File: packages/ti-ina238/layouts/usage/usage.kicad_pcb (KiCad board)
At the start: 2 copper layers, 5 parts

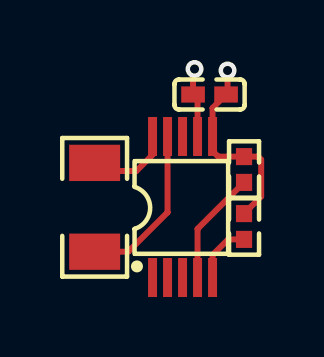
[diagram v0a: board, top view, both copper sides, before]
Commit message: ti-ina238: package update to v0.2.0, ato:^0.14.0
Build targets:
  default = rc0
  usage = rc0
Package Verify: rc0
Version: 0.1.2 -> 0.2.0
Requires ato: ^0.14.0
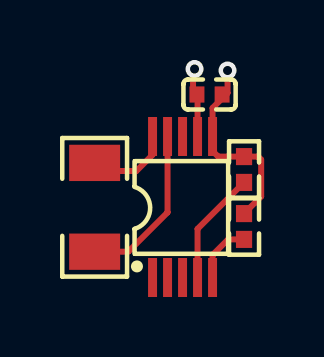
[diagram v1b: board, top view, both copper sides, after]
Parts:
- C1: value 100nF ±10% 16V X7R -> 1±10.0%F
- R1: value 16mΩ ±1% 1W -> 10000±1.0%Ω
- R2, R3: value 10kΩ ±1% 62.5mW -> 10000±1.0%Ω
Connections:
- net power_in-VCC renamed i2c_P
- net power_out-VCC renamed load_N
- C1 pad 2: GND -> lv
- U1 pad 1: address_bit_1 -> lv
- U1 pad 2: address_bit_0 -> lv
- U1 pad 7: GND -> lv
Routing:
- net GND: track 2.33 -> 0.00 mm, vias 1 -> 0
- net 1: track 0.00 -> 2.33 mm, vias 0 -> 1

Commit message: fixed literal bugs
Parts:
- removed C1: 1±10.0%F, Samsung_Electro_Mechanics_CL05B104KO5NNNC:C0402
- R1: value 10000±1.0%Ω -> 16mΩ
- R2, R3: value 10000±1.0%Ω -> 10kΩ
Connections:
- net load_N renamed INneg_N
- R1 pad 1: i2c_P -> INpos_P
- R2 pad 2: i2c_P -> hv
- R3 pad 2: i2c_P -> hv
- U1 pad 10: i2c_P -> INpos_P
- U1 pad 6: i2c_P -> hv
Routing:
- net i2c_P: track 9.54 -> 0.00 mm, vias 1 -> 0
- net hv: track 0.00 -> 9.54 mm, vias 0 -> 1
- net INpos_P: track 0.00 -> 2.33 mm, vias 0 -> 1
- net 1: track 2.33 -> 0.00 mm, vias 1 -> 0

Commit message: rebuild for frozen
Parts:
- R1: value 16mΩ -> 0.016Ω
- R2, R3: value 10kΩ -> 10000Ω
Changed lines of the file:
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@@
 	)
 	(setup
+		(stackup
+			(layer "F.SilkS"
+				(type "Top Silk Screen")
+			)
+			(layer "F.Paste"
+				(type "Top Solder Paste")
+			)
+			(layer "F.Mask"
+				(type "Top Solder Mask")
+				(color "Black")
+				(thickness 0.01)
+				(material "Solder mask")
+				(epsilon_r 3.3)
+			)
+			(layer "F.Cu"
+				(type "copper")
+				(thickness 0.035)
+			)
+			(layer "dielectric 1"
+				(type "core")
+				(thickness 1.51)
+				(material "FR4")
+				(epsilon_r 4.5)
+				(loss_tangent 0.02)
+			)
+			(layer "B.Cu"
+				(type "copper")
+				(thickness 0.035)
+			)
+			(layer "B.Mask"
+				(type "Bottom Solder Mask")
+				(color "Black")
+				(thickness 0.01)
+				(material "Solder mask")
+				(epsilon_r 3.3)
+			)
+			(layer "B.Paste"
+				(type "Bottom Solder Paste")
+			)
+			(layer "B.SilkS"
+				(type "Bottom Silk Screen")
+			)
+			(copper_finish "ENIG")
+		)
 		(pad_to_mask_clearance 0)
 		(allow_soldermask_bridges_in_footprints no)
@@
 			)
 		)
-		(property "Value" "10kΩ"
+		(property "Value" "10000Ω"
 			(at 0 4 90)
 			(layer "F.Fab")
@@
 			)
 		)
-		(property "resistance" "10±1.0%kΩ"
-			(at 0 0 0)
-			(layer "User.9")
-			(hide yes)
-		)
-		(property "max_power" "62.5mW"
+		(property "resistance" "10000±1.0%Ω"
+			(at 0 0 0)
+			(layer "User.9")
+			(hide yes)
+		)
+		(property "max_power" "0.062W"
 			(at 0 0 0)
 			(layer "User.9")
@@
 			)
 		)
-		(property "Value" "10kΩ"
+		(property "Value" "10000Ω"
 			(at 0 4 90)
 			(layer "F.Fab")
@@
 			)
 		)
-		(property "resistance" "10±1.0%kΩ"
-			(at 0 0 0)
-			(layer "User.9")
-			(hide yes)
-		)
-		(property "max_power" "62.5mW"
+		(property "resistance" "10000±1.0%Ω"
+			(at 0 0 0)
+			(layer "User.9")
+			(hide yes)
+		)
+		(property "max_power" "0.062W"
 			(at 0 0 0)
 			(layer "User.9")
@@
 			)
 		)
-		(property "Value" "16mΩ"
+		(property "Value" "0.016Ω"
 			(at 0 4 270)
 			(layer "F.Fab")
@@
 			)
 		)
-		(property "resistance" "16±1.0%mΩ"
+		(property "resistance" "0.016±1.0%Ω"
 			(at 0 0 0)
 			(layer "User.9")
@@
 			(hide yes)
 		)
-		(property "max_voltage" "any ≥0V"
-			(at 0 0 0)
-			(layer "User.9")
+		(property "max_voltage" "ℝ+V"
+			(at 0 0 0)
+			(layer "User.9")

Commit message: catching up to main
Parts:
- added C1: 100nF ±10% 16V X7R, Samsung_Electro_Mechanics_CL05B104KO5NNNC:C0402, F.Cu at (152.0, 93.0)
- R1: value 0.016Ω -> 16mΩ ±1% 1W
- R2, R3: value 10000Ω -> 10kΩ ±1% 62.5mW
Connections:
- net INneg_N renamed power_out-VCC
- R1 pad 1: INpos_P -> power_in-VCC
- R2 pad 2: hv -> power_in-VCC
- R3 pad 2: hv -> power_in-VCC
- U1 pad 1: lv -> address_bit_1
- U1 pad 10: INpos_P -> power_in-VCC
- U1 pad 2: lv -> address_bit_0
- U1 pad 6: hv -> power_in-VCC
- U1 pad 7: lv -> GND
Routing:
- net power_in-VCC: track 0.00 -> 9.54 mm, vias 0 -> 1
- net hv: track 9.54 -> 0.00 mm, vias 1 -> 0
- net INpos_P: track 2.33 -> 0.00 mm, vias 1 -> 0
- net GND: track 0.00 -> 2.33 mm, vias 0 -> 1

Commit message: fix ti-ina238
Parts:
- C1: value 100nF ±10% 16V X7R -> 1.0000000000000001e-07F
- R1: value 16mΩ ±1% 1W -> 0.016Ω
- R2, R3: value 10kΩ ±1% 62.5mW -> 10000.0Ω
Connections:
- net power_in-VCC renamed <bound method has_net_name_affix.get_prefix of <has_net_name_affix '0x45F3B.sensor.shunt_input.net_name_suffixes[0]' on <Node[Electrical] '0x45F3B.sensor.shunt_input.p.line'>>>supply<bound method has_...Electrical] '0x45F3B.sensor.shunt_input.p.line'>>>
- net power_out-VCC renamed <bound method has_net_name_affix.get_prefix of <has_net_name_affix '0x45F3B.sensor.shunt_input.net_name_suffixes[1]' on <Node[Electrical] '0x45F3B.sensor.shunt_input.n.line'>>>load<bound method has_ne...Electrical] '0x45F3B.sensor.shunt_input.n.line'>>>
- C1 pad 2: GND -> lv
- U1 pad 1: address_bit_1 -> lv
- U1 pad 2: address_bit_0 -> lv
- U1 pad 7: GND -> lv
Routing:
- net GND: track 2.33 -> 0.00 mm, vias 1 -> 0
- net 1: track 0.00 -> 2.33 mm, vias 0 -> 1

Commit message: fix ti-ina238
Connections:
- net <bound method has_net_name_affix.get_prefix of <has_net_name_affix '0x45F3B.sensor.shunt_input.net_name_suffixes[0]' on <Node[Electrical] '0x45F3B.sensor.shunt_input.p.line'>>>supply<bound method has_...Electrical] '0x45F3B.sensor.shunt_input.p.line'>>> renamed supply_P
- net <bound method has_net_name_affix.get_prefix of <has_net_name_affix '0x45F3B.sensor.shunt_input.net_name_suffixes[1]' on <Node[Electrical] '0x45F3B.sensor.shunt_input.n.line'>>>load<bound method has_ne...Electrical] '0x45F3B.sensor.shunt_input.n.line'>>> renamed load_N
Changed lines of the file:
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@@
 	)
 	(net 2 "VBUS")
-	(net 3 "<bound method has_net_name_affix.get_prefix of <has_net_name_affix '0x45F3B.sensor.shunt_input.net_name_suffixes[1]' on <Node[Electrical] '0x45F3B.sensor.shunt_input.n.line'>>>load<bound method has_ne...Electrical] '0x45F3B.sensor.shunt_input.n.line'>>>")
+	(net 3 "load_N")
 	(net 4 "ALERT")
 	(net 6 "SCL")
 	(net 7 "SDA")
-	(net 9 "<bound method has_net_name_affix.get_prefix of <has_net_name_affix '0x45F3B.sensor.shunt_input.net_name_suffixes[0]' on <Node[Electrical] '0x45F3B.sensor.shunt_input.p.line'>>>supply<bound method has_...Electrical] '0x45F3B.sensor.shunt_input.p.line'>>>")
+	(net 9 "supply_P")
 	(net 10 "lv")
 	(footprint "Samsung_Electro_Mechanics_CL05B104KO5NNNC:C0402"
@@
 			(size 0.5 0.54)
 			(layers "F.Cu" "F.Paste" "F.Mask")
-			(net 9 "<bound method has_net_name_affix.get_prefix of <has_net_name_affix '0x45F3B.sensor.shunt_input.net_name_suffixes[0]' on <Node[Electrical] '0x45F3B.sensor.shunt_input.p.line'>>>supply<bound method has_...Electrical] '0x45F3B.sensor.shunt_input.p.line'>>>")
+			(net 9 "supply_P")
 		)
 		(pad "2" smd rect
@@
 			(size 0.57 0.54)
 			(layers "F.Cu" "F.Paste" "F.Mask")
-			(net 9 "<bound method has_net_name_affix.get_prefix of <has_net_name_affix '0x45F3B.sensor.shunt_input.net_name_suffixes[0]' on <Node[Electrical] '0x45F3B.sensor.shunt_input.p.line'>>>supply<bound method has_...Electrical] '0x45F3B.sensor.shunt_input.p.line'>>>")
+			(net 9 "supply_P")
 		)
 		(embedded_fonts no)
@@
 			(size 0.3 1.3)
 			(layers "F.Cu" "F.Paste" "F.Mask")
-			(net 9 "<bound method has_net_name_affix.get_prefix of <has_net_name_affix '0x45F3B.sensor.shunt_input.net_name_suffixes[0]' on <Node[Electrical] '0x45F3B.sensor.shunt_input.p.line'>>>supply<bound method has_...Electrical] '0x45F3B.sensor.shunt_input.p.line'>>>")
+			(net 9 "supply_P")
 		)
 		(pad "7" smd rect
@@
 			(size 0.3 1.3)
 			(layers "F.Cu" "F.Paste" "F.Mask")
-			(net 3 "<bound method has_net_name_affix.get_prefix of <has_net_name_affix '0x45F3B.sensor.shunt_input.net_name_suffixes[1]' on <Node[Electrical] '0x45F3B.sensor.shunt_input.n.line'>>>load<bound method has_ne...Electrical] '0x45F3B.sensor.shunt_input.n.line'>>>")
+			(net 3 "load_N")
 		)
 		(pad "10" smd rect
@@
 			(size 0.3 1.3)
 			(layers "F.Cu" "F.Paste" "F.Mask")
-			(net 9 "<bound method has_net_name_affix.get_prefix of <has_net_name_affix '0x45F3B.sensor.shunt_input.net_name_suffixes[0]' on <Node[Electrical] '0x45F3B.sensor.shunt_input.p.line'>>>supply<bound method has_...Electrical] '0x45F3B.sensor.shunt_input.p.line'>>>")
+			(net 9 "supply_P")
 		)
 		(model "${KIPRJMOD}/../../parts/Texas_Instruments_INA238AIDGSR/VSSOP-10_L3.0-W3.0-H1.1-LS4.9-P0.50.step"
@@
 			(size 0.57 0.54)
 			(layers "F.Cu" "F.Paste" "F.Mask")
-			(net 9 "<bound method has_net_name_affix.get_prefix of <has_net_name_affix '0x45F3B.sensor.shunt_input.net_name_suffixes[0]' on <Node[Electrical] '0x45F3B.sensor.shunt_input.p.line'>>>supply<bound method has_...Electrical] '0x45F3B.sensor.shunt_input.p.line'>>>")
+			(net 9 "supply_P")
 		)
 		(embedded_fonts no)
@@
 			(size 1.21 1.7)
 			(layers "F.Cu" "F.Paste" "F.Mask")
-			(net 9 "<bound method has_net_name_affix.get_prefix of <has_net_name_affix '0x45F3B.sensor.shunt_input.net_name_suffixes[0]' on <Node[Electrical] '0x45F3B.sensor.shunt_input.p.line'>>>supply<bound method has_...Electrical] '0x45F3B.sensor.shunt_input.p.line'>>>")
+			(net 9 "supply_P")
 		)
 		(pad "2" smd rect
@@
 			(size 1.21 1.7)
 			(layers "F.Cu" "F.Paste" "F.Mask")
-			(net 3 "<bound method has_net_name_affix.get_prefix of <has_net_name_affix '0x45F3B.sensor.shunt_input.net_name_suffixes[1]' on <Node[Electrical] '0x45F3B.sensor.shunt_input.n.line'>>>load<bound method has_ne...Electrical] '0x45F3B.sensor.shunt_input.n.line'>>>")
+			(net 3 "load_N")
 		)
 		(embedded_fonts no)
